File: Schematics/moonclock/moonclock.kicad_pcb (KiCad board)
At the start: 2 copper layers, 50 x 80 mm, 31 parts, among them J1 Conn_01x05, J2 Screw_Terminal_01x04, J3 Screw_Terminal_01x03, J4 Conn_01x04, J5 Conn_01x04, U1 RP2040-Zero, U2 MCP4922-ESL, U3 MAX6071AAUT21+T, U4 MCP6002-xSN, U5 MCP7940N-xSN

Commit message: Finished Rev2 pre-gerber
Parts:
- removed the R10 at (129.2, 76.2)
- removed the R11 at (131.7, 76.2)
- removed the U2 at (123.2, 78.7)
- added C4: 100n, Capacitor_SMD:C_0805_2012Metric_Pad1.18x1.45mm_HandSolder, F.Cu at (142.1, 99.8)
- added J1: Conn_01x06, Connector_PinHeader_2.54mm:PinHeader_1x06_P2.54mm_Vertical, F.Cu at (121.0, 69.4)
- added J5: Screw_Terminal_01x04, TerminalBlock_Phoenix:TerminalBlock_Phoenix_MKDS-1,5-4-5.08_1x04_P5.08mm_Horizontal, F.Cu at (162.5, 113.1)
- added Y1: ECS-.327-6-17X-C-TR, moonclock:XTAL_ECS-.327-6-17X-C-TR, F.Cu at (145.1, 110.5)
- BT1: value Battery_Cell -> CR2032; footprint bs7:BAT_BS-7 -> moonclock:BAT_BS-7
- C2, C3: value 100n -> 6p; footprint Capacitor_SMD:C_0805_2012Metric_Pad1.18x1.45mm_HandSolder -> Capacitor_SMD:C_0603_1608Metric_Pad1.08x0.95mm_HandSolder
- J3: value Screw_Terminal_01x03 -> Screw_Terminal_01x04; footprint TerminalBlock_RND:TerminalBlock_RND_205-00233_1x03_P5.08mm_Horizontal -> TerminalBlock_Phoenix:TerminalBlock_Phoenix_MKDS-1,5-4-5.08_1x04_P5.08mm_Horizontal
- J4: renamed from J2; footprint TerminalBlock_RND:TerminalBlock_RND_205-00234_1x04_P5.08mm_Horizontal -> TerminalBlock_Phoenix:TerminalBlock_Phoenix_MKDS-1,5-4-5.08_1x04_P5.08mm_Horizontal
- U3: value MAX6071AAUT21+T -> MCP47FVB22-E/ST; footprint Package_TO_SOT_SMD:SOT-23-6 -> Package_SO:TSSOP-8_4.4x3mm_P0.65mm
- moved U4 80.1 mm to (146.6, 101.5), turned to 90 degrees
- moved BT1 65.6 mm to (152.2, 127.4)
- moved C3 45.7 mm to (149.6, 108.7)
- moved J3 42.4 mm to (123.1, 113.7)
- moved C2 40.2 mm to (140.6, 108.7), turned to -90 degrees
- moved U3 33.3 mm to (136.5, 99.5), turned to -90 degrees
- moved C5 20.8 mm to (139.9, 99.8), turned to -90 degrees
- moved R10 19.5 mm to (132.8, 99.3), turned to 90 degrees
- moved JP2 15.7 mm to (130.2, 99.3), turned to 90 degrees
- moved J4 15.4 mm to (123.1, 93.4), turned to -90 degrees
- moved R9 4.05 mm to (136.8, 93.2), turned to 180 degrees
- moved R8 3.85 mm to (136.8, 89.0), turned to 180 degrees
- moved R5 2.75 mm to (146.8, 87.9)
- moved R6 2.75 mm to (149.2, 87.9)
- moved R11 0.25 mm to (131.0, 93.7)
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- renumbered C4 to C5, J5 to J2, J4 to J6, J1 to J7, JP2 to JP1, JP1 to JP2, R5 to R10, R4 to R11, R2 to R12, R9 to R2, R7 to R3, R8 to R4, R12 to R5, R13 to R6, R14 to R7, R6 to R8, R3 to R9, U4 to U2, U5 to U4
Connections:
- C2 pad 1: VREF_2048 -> Net-(U5-X1)
- C3 pad 1: +3.3V -> Net-(U5-X2)
- J3 pad 2: RIGHT_BUT -> GND
- J3 pad 3: GND -> RIGHT_BUT
- U1 pad 15: DAC_SCK -> EXP4
- U1 pad 16: DAC_MOSI -> EXP3
- U1 pad 17: DAC_CS -> EXP2
- U1 pad 18: DAC_LDAC -> EXP1
- U1 pad 5: RIGHT_BUT -> unconnected-(U1-GP4-Pad5)
- U1 pad 8: unconnected-(U1-GP7-Pad8) -> RIGHT_BUT
- U3 pad 1: GND -> +3.3V
- U3 pad 2: GND -> +3.3V
- U3 pad 3: +3.3V -> /M1_DAC
- U3 pad 4: +3.3V -> /M2_DAC
- U3 pad 5: VREF_2048 -> GND
- U3 pad 6: VREF_2048 -> GND
- U4 pad 1: unconnected-(U5-X1-Pad1) -> Net-(U5-X1)
- U4 pad 2: unconnected-(U5-X2-Pad2) -> Net-(U5-X2)
- U4 pad 4: unconnected-(U5-VSS-Pad4) -> GND
- U4 pad 5: unconnected-(U5-SDA-Pad5) -> I2C1_SDA
- U4 pad 6: unconnected-(U5-SCL-Pad6) -> I2C1_SCL
- U4 pad 8: unconnected-(U5-VCC-Pad8) -> +3.3V
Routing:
- net GND: track 200.8 -> 293.2 mm, vias 44 -> 51
- net EXP1: track 0.00 -> 87.3 mm, vias 0 -> 2
- net EXP2: track 0.00 -> 76.1 mm, vias 0 -> 2
- net LEFT_BUT: track 19.2 -> 76.5 mm, vias 0 -> 1
- net RIGHT_BUT: track 38.7 -> 80.0 mm, vias 2 -> 1
- net Net-(BT1-+): track 0.00 -> 36.4 mm, vias 0 -> 2
- net I2C1_SCL: track 16.2 -> 44.0 mm, vias 0 -> 2
- net DAC_LDAC: track 26.2 -> 0.00 mm, vias 2 -> 0
- net EXP4: track 0.00 -> 24.7 mm
- net EXP3: track 0.00 -> 22.7 mm
- net I2C1_SDA: track 23.6 -> 44.8 mm, vias 0 -> 3
- net VREF_2048: track 20.3 -> 0.00 mm, vias 3 -> 0
- net DAC_CS: track 20.0 -> 0.00 mm, vias 2 -> 0
- net Net-(JP1-B): track 26.3 -> 9.06 mm
- net /M1_DAC: track 21.1 -> 4.29 mm, vias 2 -> 0
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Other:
- board text added: "2025 Tennessee Carmel-Veilleux"
- board text added: "3V3"
- board text added: "CAL"
- board text added: "EXP1"
- board text added: "EXP2"
- board text added: "EXP3"
- board text added: "EXP4"
- board text added: "MoonClock V1.0 Rev 2"
- board text added: "SCL"
- board text added: "SDA"
- board text removed: "Tennessee Carmel-Veilleux 2025"

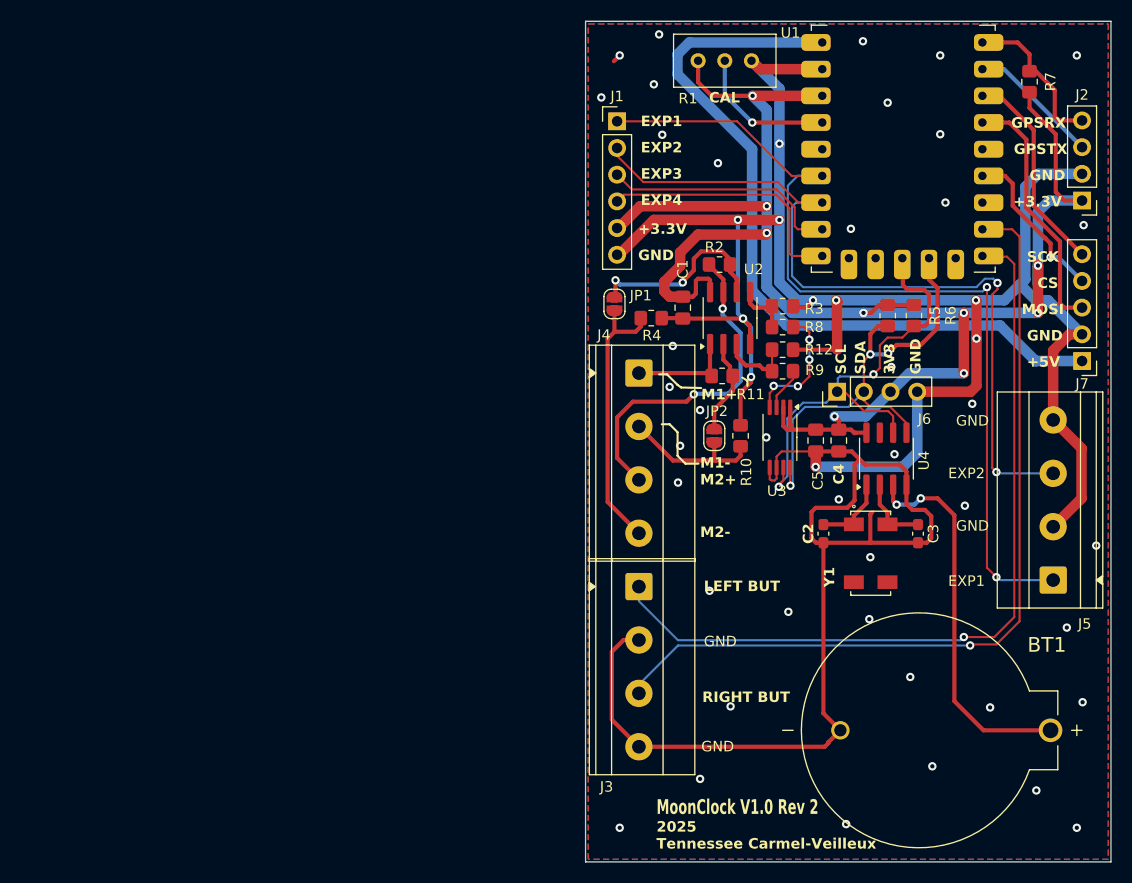
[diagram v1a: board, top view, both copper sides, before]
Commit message: Fix footprint for U1 and corner vias
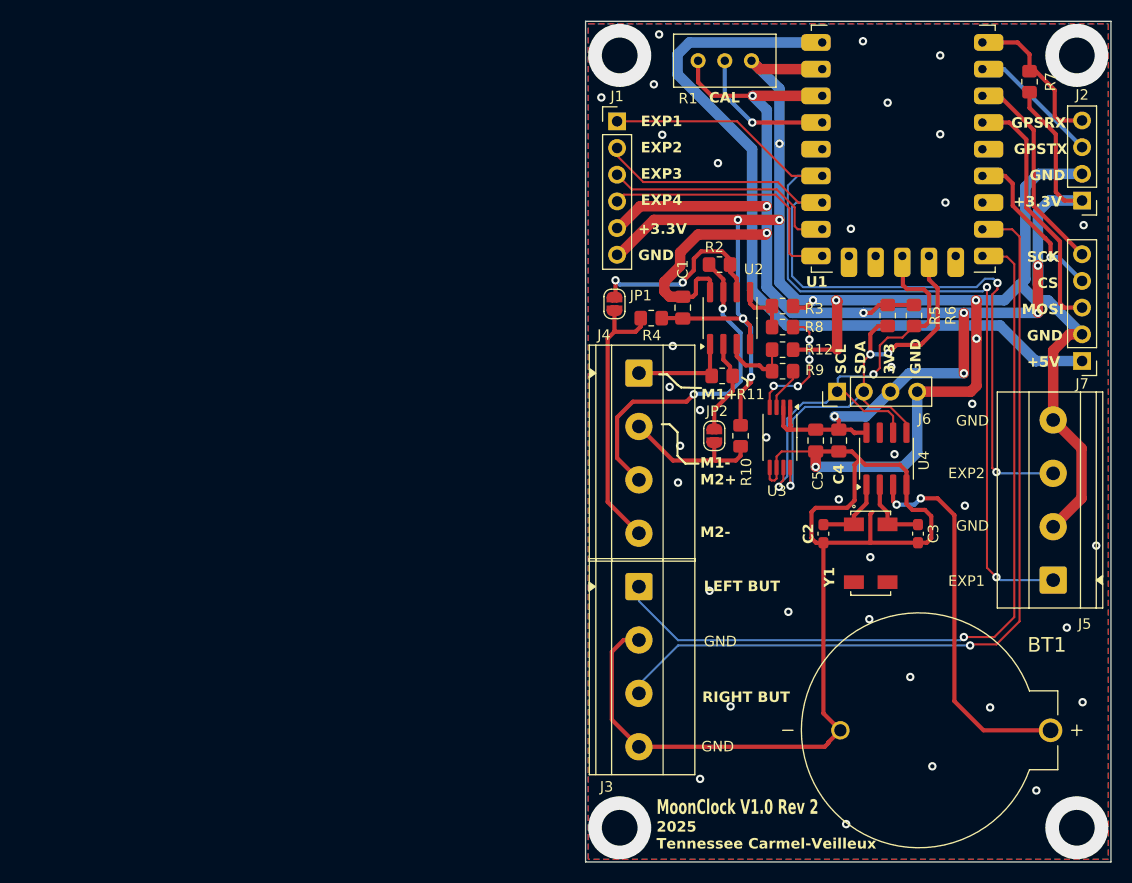
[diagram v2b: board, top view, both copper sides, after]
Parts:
- U1: footprint rp2040-zero:RP2040-Zero -> moonclock:RP2040-Zero
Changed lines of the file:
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@@
 		)
 	)
-	(footprint "rp2040-zero:RP2040-Zero"
+	(footprint "moonclock:RP2040-Zero"
 		(layer "F.Cu")
 		(at 137.985 84.775)
 		(property "Reference" "U1"
-			(at 10.16 -15.45 0)
+			(at 2.015 -0.075 0)
 			(unlocked yes)
-			(layer "F.Fab")
+			(layer "F.SilkS")
 			(effects
 				(font
 					(size 1 1)
-					(thickness 0.15)
+					(thickness 0.2)
+					(bold yes)
 				)
 			)
 		)
 		(property "Value" "RP2040-Zero"
-			(at 10.715 -17.625 0)
+			(at 10.16 -13.45 0)
 			(unlocked yes)
 			(layer "F.Fab")
@@
 			(layer "F.Fab")
 		)
-		(fp_text user "${REFERENCE}"
-			(at -0.485 -23.775 0)
-			(unlocked yes)
-			(layer "F.SilkS")
-			(effects
-				(font
-					(size 1 1)
-					(thickness 0.2)
-				)
-			)
-		)
 		(pad "1" thru_hole roundrect
 			(at 17.78 -22.86)
@@
 		)
 		(pad "10" thru_hole roundrect
-			(at 15.24 -2.33)
+			(at 15.24 -2.54)
 			(size 1.6 2.8)
 			(drill 0.8
@@
 		)
 		(pad "11" thru_hole roundrect
-			(at 12.7 -2.33)
+			(at 12.7 -2.54)
 			(size 1.5748 2.8)
 			(drill 0.8
@@
 		)
 		(pad "12" thru_hole roundrect
-			(at 10.16 -2.33)
+			(at 10.16 -2.54)
 			(size 1.5748 2.8)
 			(drill 0.8
@@
 		)
 		(pad "13" thru_hole roundrect
-			(at 7.62 -2.33)
+			(at 7.62 -2.54)
 			(size 1.5748 2.8)
 			(drill 0.8
@@
 		)
 		(pad "14" thru_hole roundrect
-			(at 5.08 -2.33)
+			(at 5.08 -2.54)
 			(size 1.5748 2.8)
 			(drill 0.8
@@
 	(via
 		(at 164.75 63.15)
-		(size 0.8)
-		(drill 0.4)
+		(size 6)
+		(drill 3.4)
 		(layers "F.Cu" "B.Cu")
 		(free yes)
@@
 	(via
 		(at 121.25 63.15)
-		(size 0.8)
-		(drill 0.4)
+		(size 6)
+		(drill 3.4)
 		(layers "F.Cu" "B.Cu")
 		(free yes)
@@
 	(via
 		(at 164.75 136.65)
-		(size 0.8)
-		(drill 0.4)
+		(size 6)
+		(drill 3.4)
 		(layers "F.Cu" "B.Cu")
 		(free yes)
@@
 	(via
 		(at 121.25 136.65)
-		(size 0.8)
-		(drill 0.4)
-		(layers "F.Cu" "B.Cu")
-		(net 1)
+		(size 6)
+		(drill 3.4)
+		(layers "F.Cu" "B.Cu")
+		(net 1)
